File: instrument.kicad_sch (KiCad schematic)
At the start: 49 parts, among them J10 SPARE, J11 2x5 2.56mm RA, J12 RJ45, J13 USB-B1HSB6, J17 691322310004, J5 4 Pins 5.08mm, J6 OSCILLOSCOPE, J7 OSCILLOSCOPE, J8 6 pins 3.81mm, J9 AWG

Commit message: First try to fit electronic on PCB
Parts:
- TP78: renamed from TP251; footprint Connector_PinHeader_2.54mm:PinHeader_1x01_P2.54mm_Horizontal -> Connector_Pin:Pin_D1.0mm_L10.0mm
- TP79: renamed from TP23; footprint Connector_PinHeader_2.54mm:PinHeader_1x01_P2.54mm_Horizontal -> Connector_Pin:Pin_D1.0mm_L10.0mm
- TP80: renamed from TP252; footprint Connector_PinHeader_2.54mm:PinHeader_1x01_P2.54mm_Horizontal -> Connector_Pin:Pin_D1.0mm_L10.0mm
- TP81: renamed from TP253; footprint Connector_PinHeader_2.54mm:PinHeader_1x01_P2.54mm_Horizontal -> Connector_Pin:Pin_D1.0mm_L10.0mm
- TP82: renamed from TP254; footprint Connector_PinHeader_2.54mm:PinHeader_1x01_P2.54mm_Horizontal -> Connector_Pin:Pin_D1.0mm_L10.0mm
- TP83: renamed from TP177; footprint Connector_PinHeader_2.54mm:PinHeader_1x01_P2.54mm_Horizontal -> Connector_Pin:Pin_D1.0mm_L10.0mm
- TP84: renamed from TP178; footprint Connector_PinHeader_2.54mm:PinHeader_1x01_P2.54mm_Horizontal -> Connector_Pin:Pin_D1.0mm_L10.0mm
- TP85: renamed from TP179; footprint Connector_PinHeader_2.54mm:PinHeader_1x01_P2.54mm_Horizontal -> Connector_Pin:Pin_D1.0mm_L10.0mm
- TP86: renamed from TP249; footprint Connector_PinHeader_2.54mm:PinHeader_1x01_P2.54mm_Horizontal -> Connector_Pin:Pin_D1.0mm_L10.0mm
- TP87: renamed from TP180; footprint Connector_PinHeader_2.54mm:PinHeader_1x01_P2.54mm_Horizontal -> Connector_Pin:Pin_D1.0mm_L10.0mm
- TP88: renamed from TP250; footprint Connector_PinHeader_2.54mm:PinHeader_1x01_P2.54mm_Horizontal -> Connector_Pin:Pin_D1.0mm_L10.0mm
- renumbered D87 to D30, D88 to D31, D89 to D32, D90 to D33, J5 to J17, J6 to J18, J7 to J19, J8 to J20, J9 to J21, J10 to J22, J17 to J23, J12 to J24, J13 to J25, J11 to J26, NT436 to NT446, NT437 to NT447, NT438 to NT448, NT439 to NT449, NT440 to NT450, NT441 to NT451, NT442 to NT452, NT443 to NT453, NT584 to NT454, NT444 to NT455, NT585 to NT456, NT450 to NT457, NT452 to NT458, NT455 to NT459, NT445 to NT460, NT446 to NT461, NT447 to NT462, NT448 to NT463, NT449 to NT464, NT451 to NT465, NT453 to NT466, NT454 to NT467, R136 to R66, R137 to R67

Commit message: backup 1 bank done
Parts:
- NT446, NT447, NT448, NT449, NT450, NT451, NT452, NT453, NT454, NT455, NT456, NT457, NT458, NT459, NT460, NT461, NT462, NT463, NT464, NT465, NT466, NT467: footprint NetTie:NetTie-2_THT_Pad1.0mm -> NetTie:NetTie-2_Front1.0mm
- TP78, TP79, TP80, TP81, TP82, TP83, TP84, TP85, TP86, TP87, TP88: footprint Connector_Pin:Pin_D1.0mm_L10.0mm -> Connector_Pin:Pin_D0.9mm_L10.0mm_W2.4mm_FlatFork

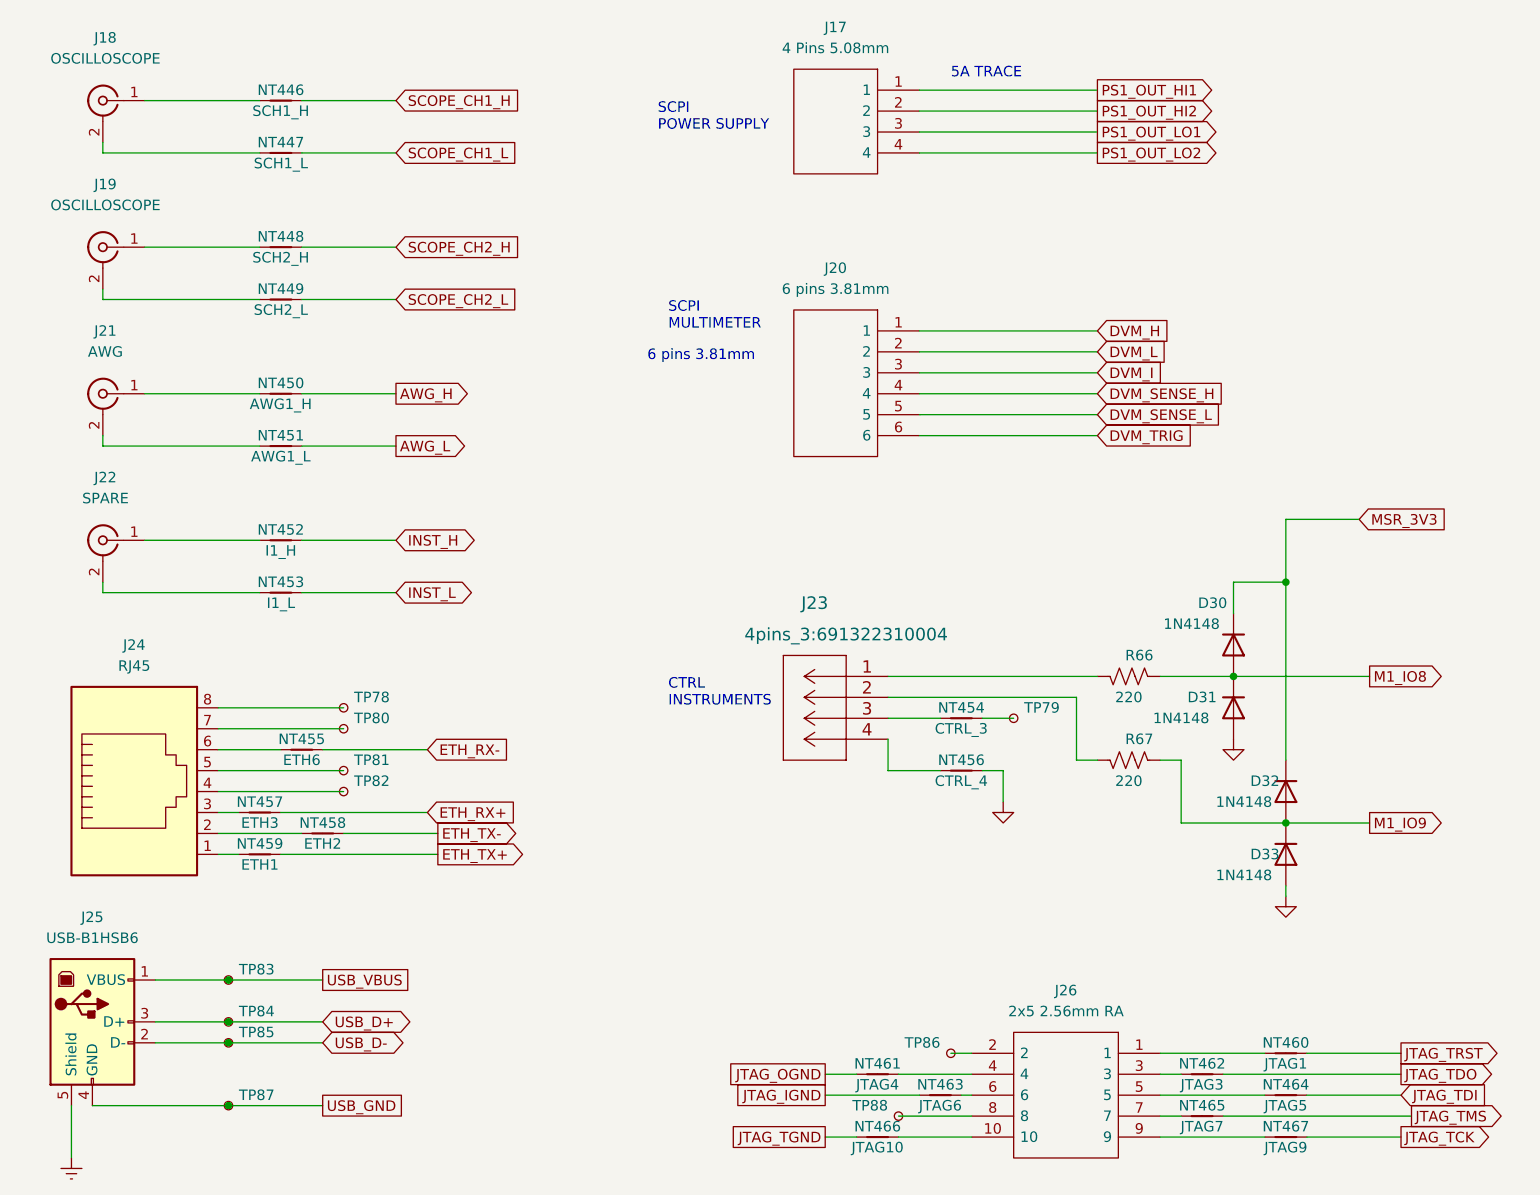
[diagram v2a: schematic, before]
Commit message: half PCB completed
FTS io controller PCB
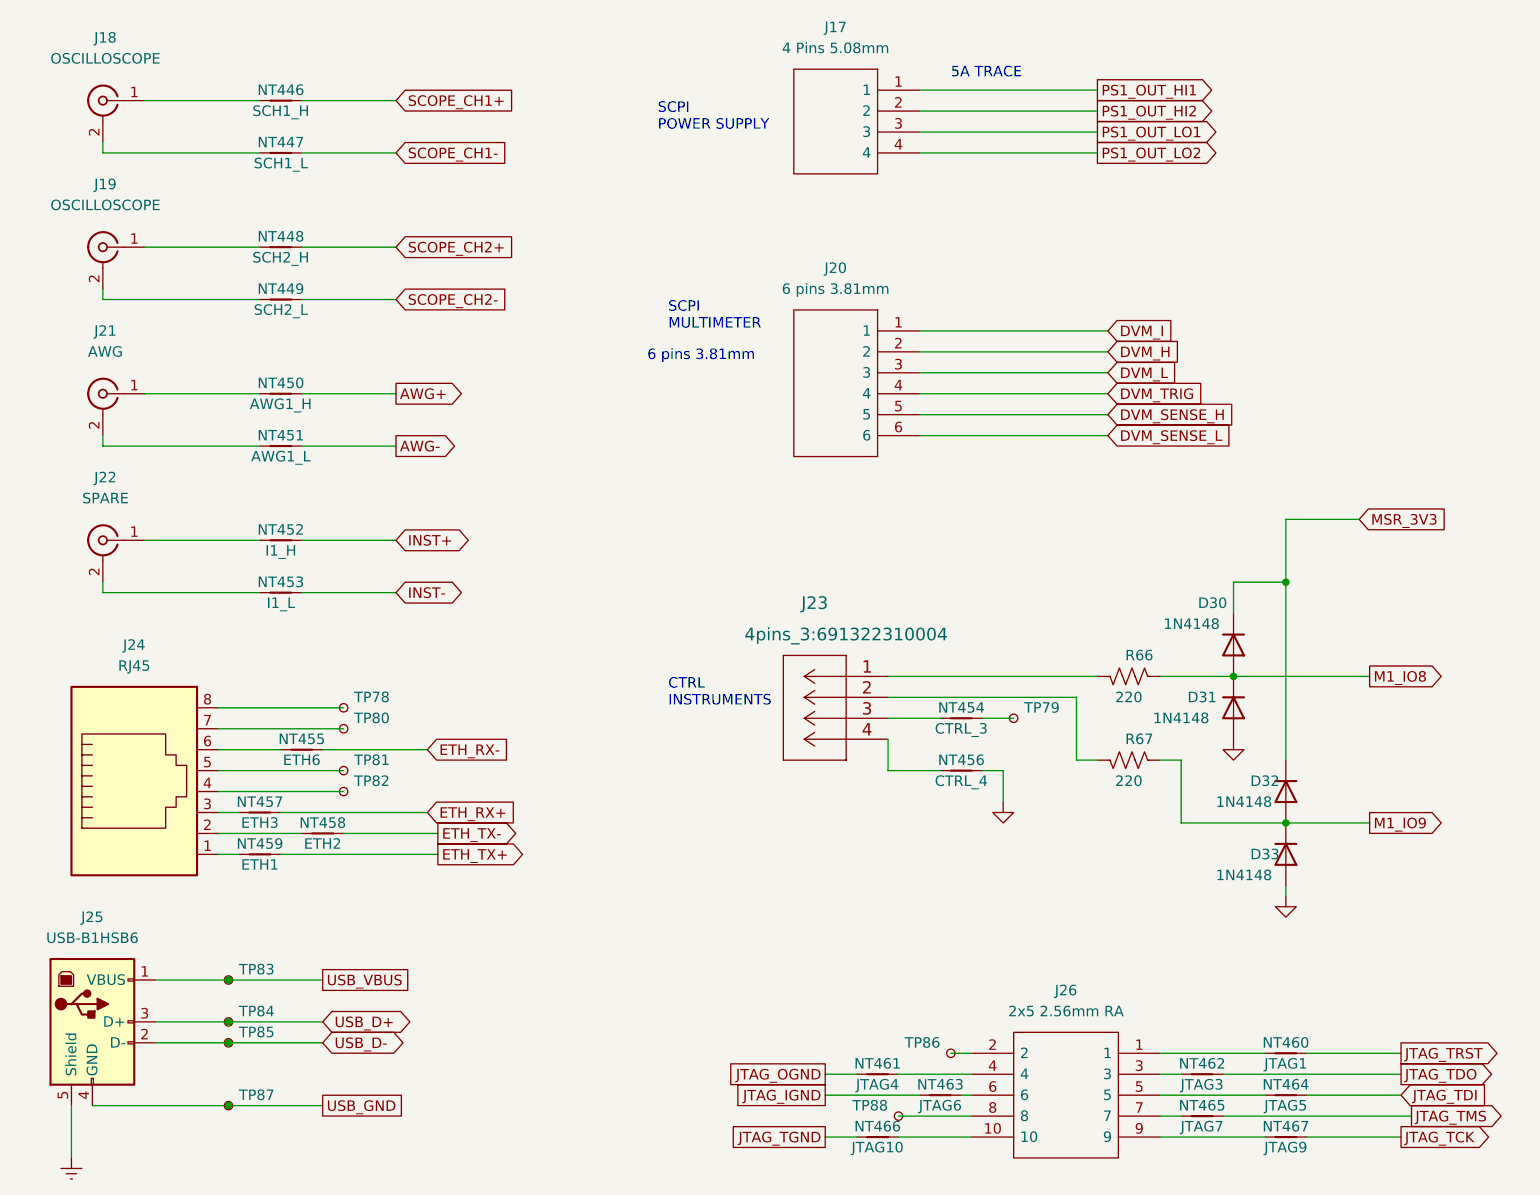
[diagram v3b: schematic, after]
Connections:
- net DVM_H: now also J20.2; no longer J20.1
- net DVM_I: now also J20.1; no longer J20.3
- net DVM_L: now also J20.3; no longer J20.2
- net DVM_SENSE_H: now also J20.5; no longer J20.4
- net DVM_SENSE_L: now also J20.6; no longer J20.5
- net DVM_TRIG: now also J20.4; no longer J20.6
- net AWG_H renamed AWG+
- net AWG_L renamed AWG-
- net INST_H renamed INST+
- net INST_L renamed INST-
- net SCOPE_CH1_H renamed SCOPE_CH1+
- net SCOPE_CH1_L renamed SCOPE_CH1-
- net SCOPE_CH2_H renamed SCOPE_CH2+
- net SCOPE_CH2_L renamed SCOPE_CH2-

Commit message: PCB Completed
PCB completed but final verification not completed
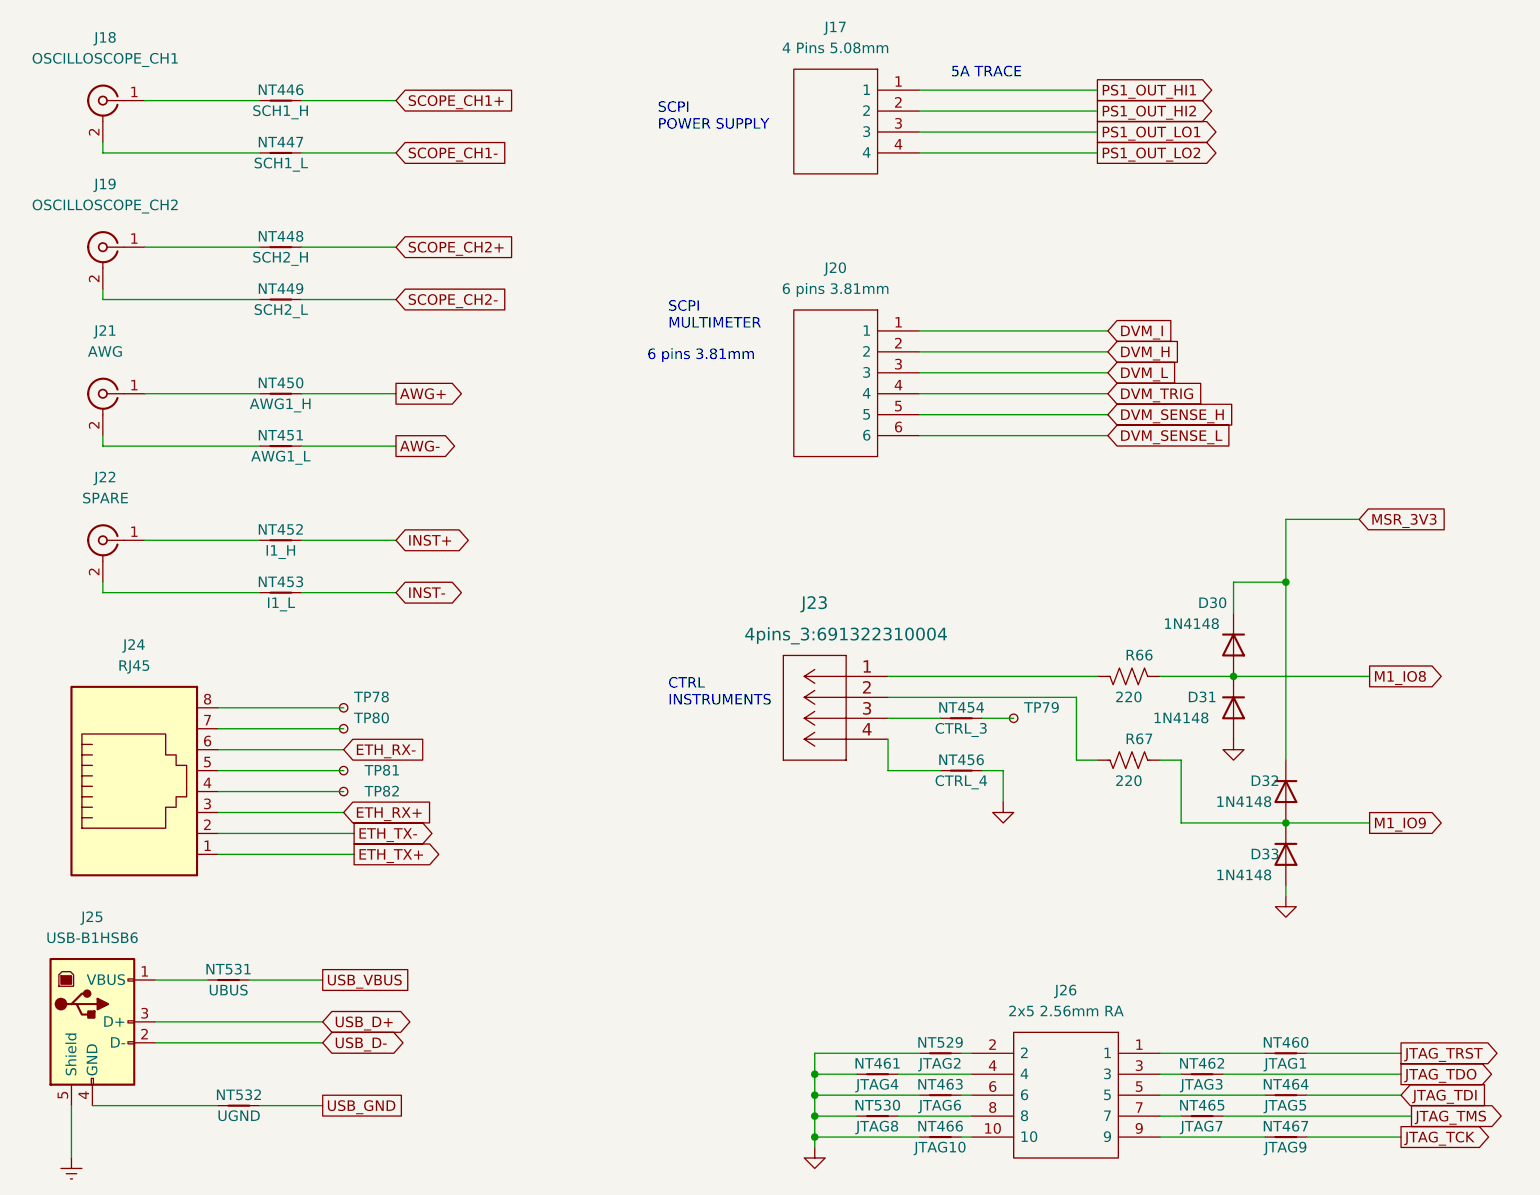
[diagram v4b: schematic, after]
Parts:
- removed NT455: ETH6, NetTie:NetTie-2_Front1.0mm, symbol Device:NetTie_2
- removed NT457: ETH3, NetTie:NetTie-2_Front1.0mm, symbol Device:NetTie_2
- removed NT458: ETH2, NetTie:NetTie-2_Front1.0mm, symbol Device:NetTie_2
- removed NT459: ETH1, NetTie:NetTie-2_Front1.0mm, symbol Device:NetTie_2
- removed TP83, TP84, TP85, TP86, TP87, TP88: TestPoint_Small, Connector_Pin:Pin_D0.9mm_L10.0mm_W2.4mm_FlatFork, symbol Connector:TestPoint_Small
- added NT529: JTAG2, NetTie:NetTie-2_Front1.0mm, symbol Device:NetTie_2
- added NT530: JTAG8, NetTie:NetTie-2_Front1.0mm, symbol Device:NetTie_2
- added NT531: UBUS, NetTie:NetTie-2_Front1.0mm, symbol Device:NetTie_2
- added NT532: UGND, NetTie:NetTie-2_Front1.0mm, symbol Device:NetTie_2
- J18: value OSCILLOSCOPE -> OSCILLOSCOPE_CH1; footprint Connector_Coaxial:BNC_Amphenol_B6252HB-NPP3G-50_Horizontal -> BNC:TE_1-1337542-0
- J19: value OSCILLOSCOPE -> OSCILLOSCOPE_CH2; footprint Connector_Coaxial:BNC_Amphenol_B6252HB-NPP3G-50_Horizontal -> BNC:TE_1-1337542-0
- J21, J22: footprint Connector_Coaxial:BNC_Amphenol_B6252HB-NPP3G-50_Horizontal -> BNC:TE_1-1337542-0
- TP78, TP79, TP80, TP81, TP82: footprint Connector_Pin:Pin_D0.9mm_L10.0mm_W2.4mm_FlatFork -> TestPoint:TestPoint_THTPad_D1.5mm_Drill0.7mm
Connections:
- net JTAG_IGND is gone; now on net GND: NT463.1
- net JTAG_OGND is gone; now on net GND: NT461.1
- net JTAG_TGND is gone; now on net GND: NT466.1
- net ETH_RX+: now also J24.3
- net ETH_RX-: now also J24.6
- net ETH_TX+: now also J24.1
- net ETH_TX-: now also J24.2
- net GND: now also NT529.1, NT530.1
- net USB_GND: now also NT532.2; no longer J25.4 (GND)
- net USB_VBUS: now also NT531.2; no longer J25.1 (VBUS)
- net at J26.2: now also NT529.2
- net at J26.8: now also NT530.2
- new net: J25.1 (VBUS), NT531.1
- new net: J25.4 (GND), NT532.1
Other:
- moved on the sheet: NT466

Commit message: PCB completed
All modification made
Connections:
- net M1_IO8: now also D32.2 (A), D33.1 (K), R67.1; no longer D30.2 (A), D31.1 (K), R66.1
- net M1_IO9: now also D30.2 (A), D31.1 (K), R66.1; no longer D32.2 (A), D33.1 (K), R67.1
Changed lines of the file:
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@@
     )
   )
-  (global_label "M1_IO8" (shape output) (at 199.39 97.79 0) (fields_autoplaced)
+  (global_label "M1_IO9" (shape output) (at 199.39 97.79 0) (fields_autoplaced)
     (effects (font (size 1.27 1.27)) (justify left))
     (property "Intersheet References" "${INTERSHEET_REFS}" (id 0) (at 208.5764 97.7106 0)
@@
     )
   )
-  (global_label "M1_IO9" (shape output) (at 199.39 115.57 0) (fields_autoplaced)
+  (global_label "M1_IO8" (shape output) (at 199.39 115.57 0) (fields_autoplaced)
     (effects (font (size 1.27 1.27)) (justify left))
     (property "Intersheet References" "${INTERSHEET_REFS}" (id 0) (at 208.5764 115.4906 0)

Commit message: update
Correction of small error
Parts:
- J23: value 691322310004 -> 4 pins 3.81mm
- J24: footprint Connector_RJ:RJ45_Amphenol_54602-x08_Horizontal -> Connector_RJ:RJ45_Ninigi_GE
- J26: value 2x5 2.56mm RA -> 2x5 2.54mm RA
- R66, R67: footprint Resistor_THT:R_Axial_DIN0309_L9.0mm_D3.2mm_P12.70mm_Horizontal -> Resistor_THT:R_Axial_DIN0207_L6.3mm_D2.5mm_P10.16mm_Horizontal
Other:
- note added: "4 pins 3.81mm"
- note removed: "6 pins 3.81mm"
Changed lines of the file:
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@@
     (effects (font (size 1.27 1.27)) (justify left bottom))
   )
+  (text "4 pins 3.81mm" (at 124.46 92.71 0)
+    (effects (font (size 1.27 1.27)) (justify left bottom))
+  )
   (text "SCPI\nMULTIMETER" (at 114.3 55.88 0)
-    (effects (font (size 1.27 1.27)) (justify left bottom))
-  )
-  (text "6 pins 3.81mm" (at 111.76 59.69 0)
     (effects (font (size 1.27 1.27)) (justify left bottom))
   )
@@
     (property "Reference" "R66" (id 0) (at 171.45 95.25 90))
     (property "Value" "220" (id 1) (at 170.18 100.33 90))
-    (property "Footprint" "Resistor_THT:R_Axial_DIN0309_L9.0mm_D3.2mm_P12.70mm_Horizontal" (id 2) (at 169.926 96.774 90)
+    (property "Footprint" "Resistor_THT:R_Axial_DIN0207_L6.3mm_D2.5mm_P10.16mm_Horizontal" (id 2) (at 169.926 96.774 90)
       (effects (font (size 1.27 1.27)) hide)
     )
@@
     (property "Reference" "J24" (id 0) (at 49.53 93.98 0))
     (property "Value" "RJ45" (id 1) (at 49.53 96.52 0))
-    (property "Footprint" "Connector_RJ:RJ45_Amphenol_54602-x08_Horizontal" (id 2) (at 49.53 111.125 90)
+    (property "Footprint" "Connector_RJ:RJ45_Ninigi_GE" (id 2) (at 49.53 111.125 90)
       (effects (font (size 1.27 1.27)) hide)
     )
@@
     (in_bom yes) (on_board yes) (fields_autoplaced)
     (property "Reference" "J26" (id 0) (at 162.56 135.89 0))
-    (property "Value" "2x5 2.56mm RA" (id 1) (at 162.56 138.43 0))
+    (property "Value" "2x5 2.54mm RA" (id 1) (at 162.56 138.43 0))
     (property "Footprint" "Connector_jtag:SHDRRA10W64P254_2X5_1270X910X880P" (id 2) (at 154.94 140.97 0)
       (effects (font (size 1.27 1.27)) (justify left) hide)
@@
     (property "Reference" "R67" (id 0) (at 171.45 105.41 90))
     (property "Value" "220" (id 1) (at 170.18 110.49 90))
-    (property "Footprint" "Resistor_THT:R_Axial_DIN0309_L9.0mm_D3.2mm_P12.70mm_Horizontal" (id 2) (at 169.926 106.934 90)
+    (property "Footprint" "Resistor_THT:R_Axial_DIN0207_L6.3mm_D2.5mm_P10.16mm_Horizontal" (id 2) (at 169.926 106.934 90)
       (effects (font (size 1.27 1.27)) hide)
     )
@@
       (effects (font (size 1.524 1.524)))
     )
-    (property "Value" "691322310004" (id 1) (at 132.08 92.71 0)
+    (property "Value" "4 pins 3.81mm" (id 1) (at 132.08 92.71 0)
       (effects (font (size 1.524 1.524)) hide)
     )
     (property "Footprint" "4pins_3:691322310004" (id 2) (at 135.89 92.71 0)
-      (effects (font (size 1.524 1.524)))
+      (effects (font (size 1.524 1.524)) hide)
     )
     (property "Datasheet" "" (id 3) (at 140.97 97.79 0)
